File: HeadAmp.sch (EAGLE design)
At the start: 31 parts, among them U1 MAX97220A

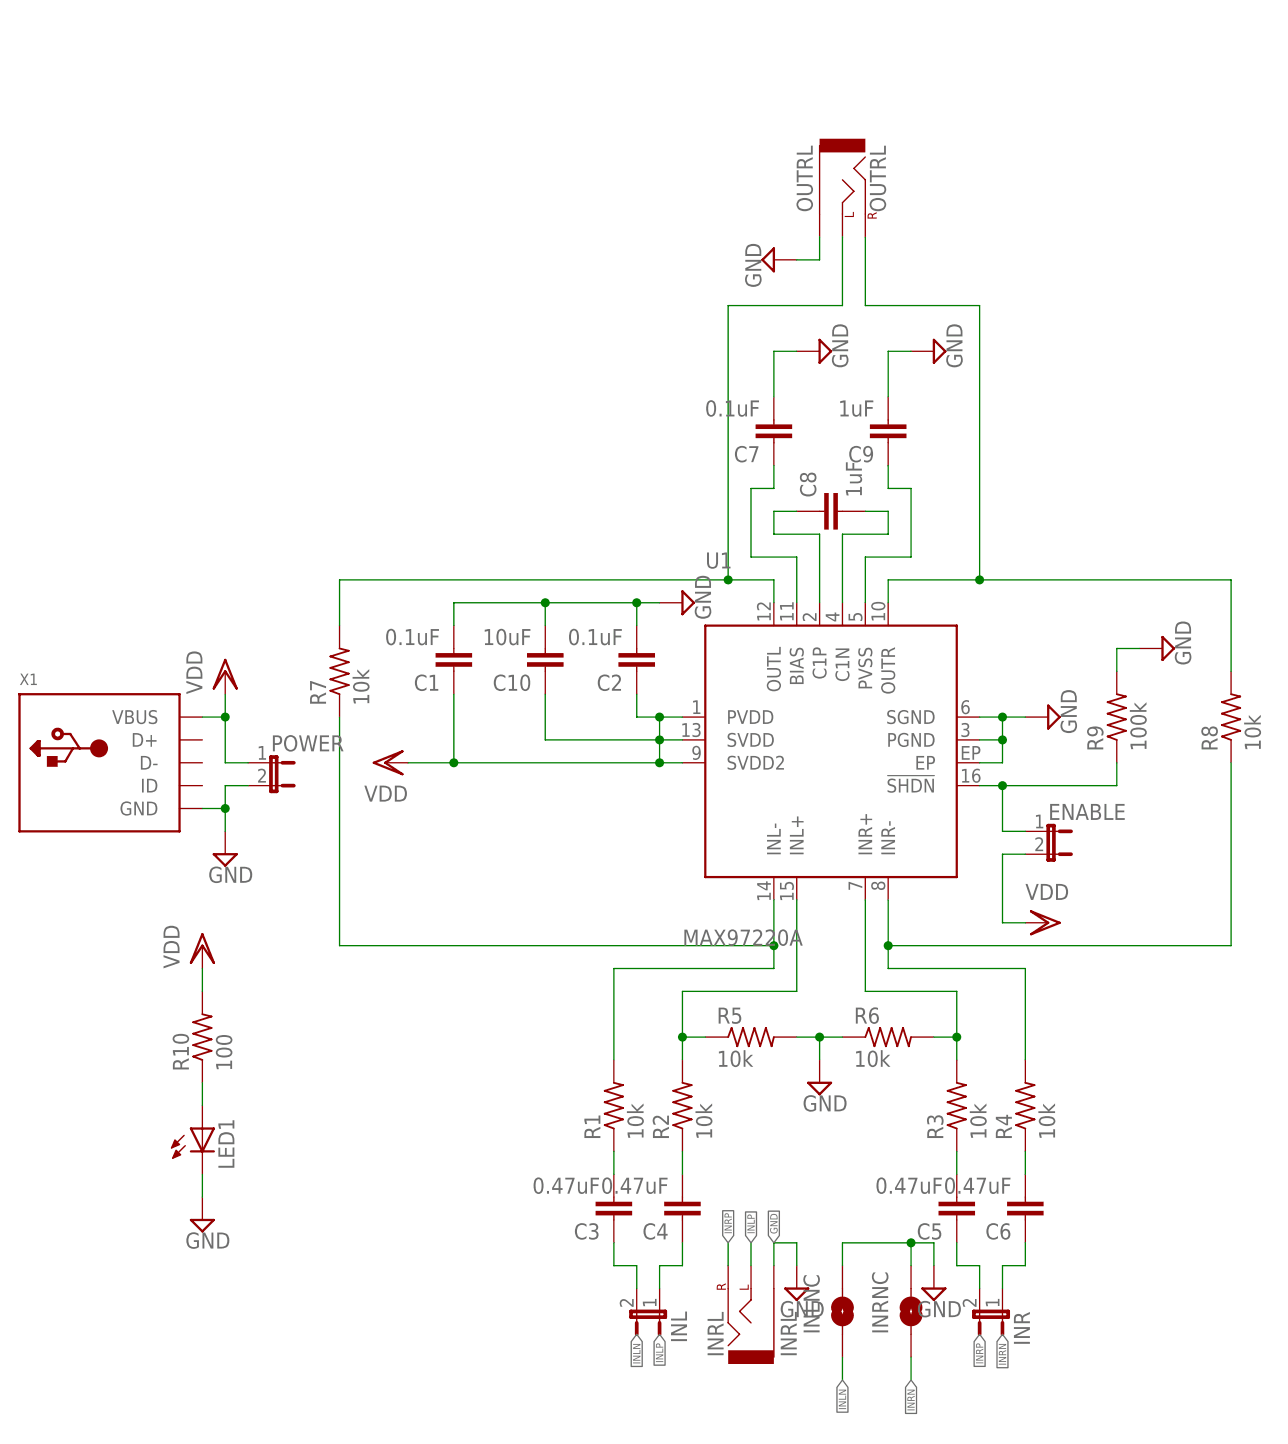
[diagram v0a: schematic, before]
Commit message: Changed Gain to Max
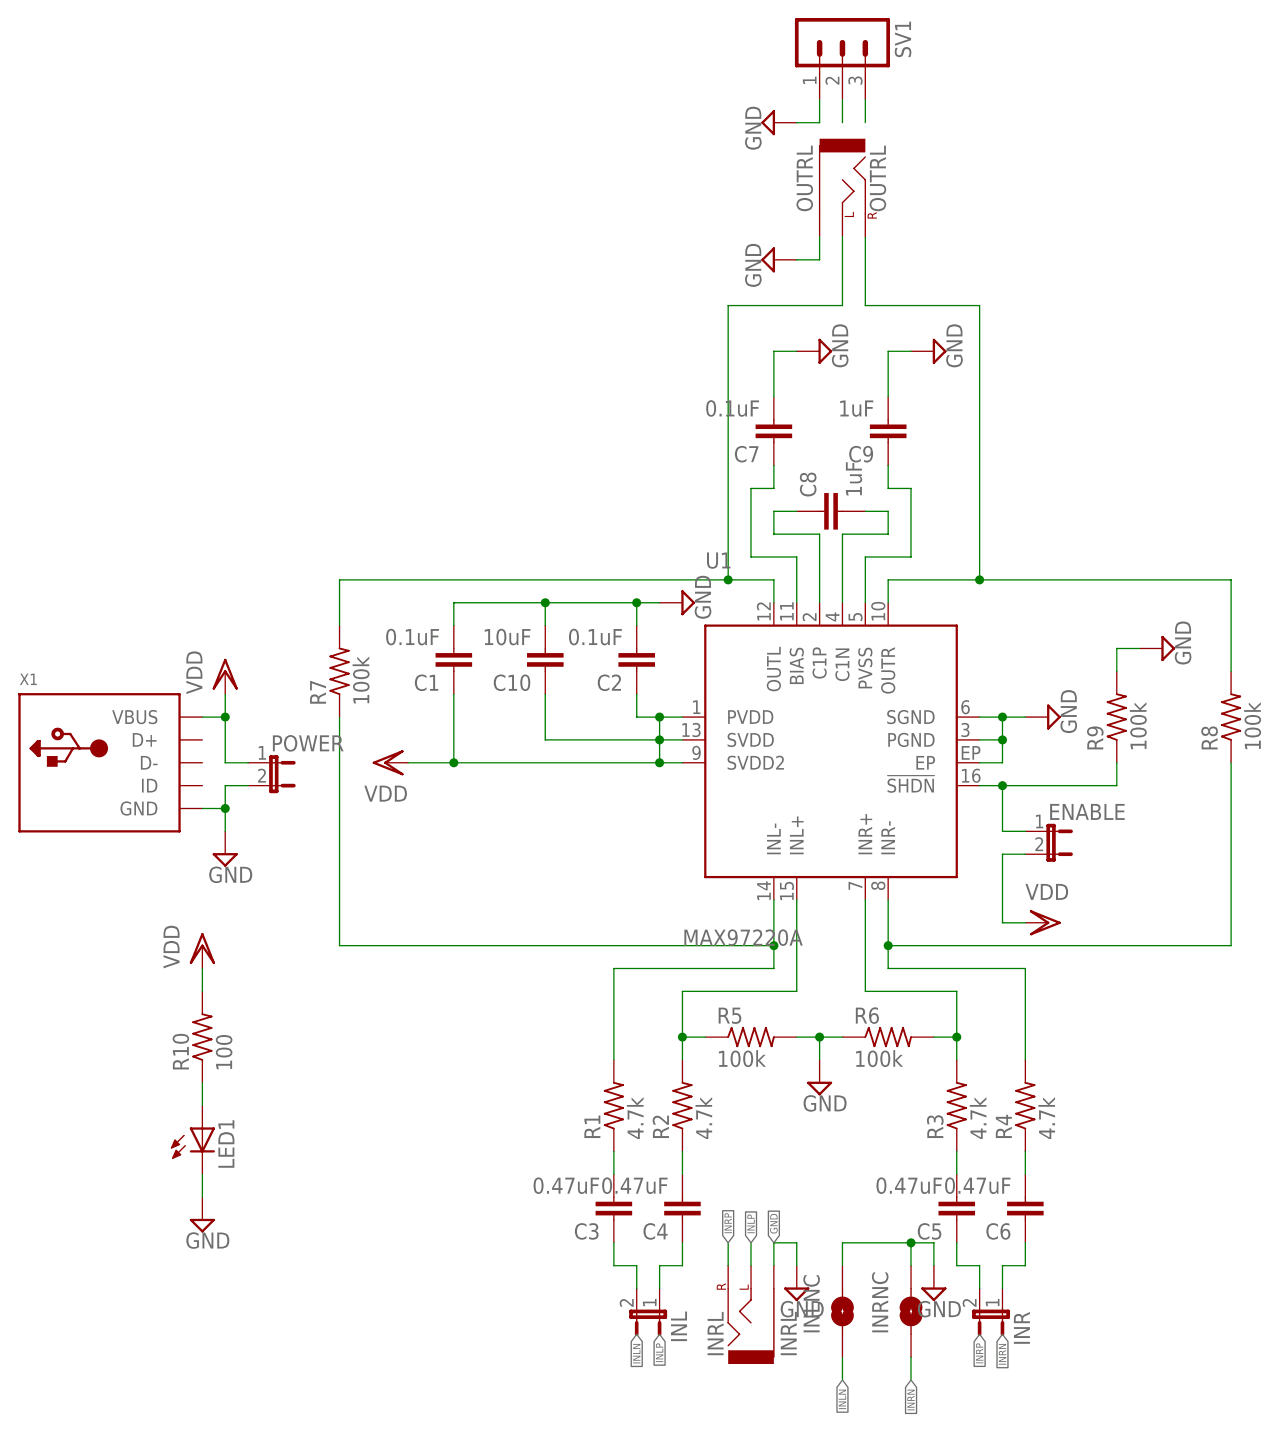
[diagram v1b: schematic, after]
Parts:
- added SV1: (no value), con-lstb:MA03-1
- R1, R2, R3, R4: value 10k -> 4.7k
- R5, R6, R7, R8: value 10k -> 100k
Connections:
- removed net N$5: OUTRL.1, R8.2, U1.OUTR
- removed net N$6: OUTRL.4, R7.2, U1.OUTL
- new net LOUT: OUTRL.4, R7.2, SV1.2, U1.OUTL
- new net ROUT: OUTRL.1, R8.2, SV1.3, U1.OUTR
- net GND: now also SV1.1
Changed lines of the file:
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@@
 <setting verticaltext="up"/>
 </settings>
-<grid distance="0.1" unitdist="inch" unit="inch" style="lines" multiple="1" display="yes" altdistance="0.01" altunitdist="inch" altunit="inch"/>
+<grid distance="0.1" unitdist="inch" unit="inch" style="lines" multiple="1" display="no" altdistance="0.01" altunitdist="inch" altunit="inch"/>
 <layers>
 <layer number="1" name="Top" color="4" fill="1" visible="no" active="no"/>
@@
 <parts>
 <part name="U1" library="maxim" deviceset="MAX97220A" device=""/>
-<part name="R1" library="rcl" deviceset="R-US_" device="R0603" value="10k"/>
-<part name="R2" library="rcl" deviceset="R-US_" device="R0603" value="10k"/>
-<part name="R3" library="rcl" deviceset="R-US_" device="R0603" value="10k"/>
-<part name="R4" library="rcl" deviceset="R-US_" device="R0603" value="10k"/>
-<part name="R5" library="rcl" deviceset="R-US_" device="R0603" value="10k"/>
-<part name="R6" library="rcl" deviceset="R-US_" device="R0603" value="10k"/>
-<part name="R7" library="rcl" deviceset="R-US_" device="R0603" value="10k"/>
-<part name="R8" library="rcl" deviceset="R-US_" device="R0603" value="10k"/>
+<part name="R1" library="rcl" deviceset="R-US_" device="R0603" value="4.7k"/>
+<part name="R2" library="rcl" deviceset="R-US_" device="R0603" value="4.7k"/>
+<part name="R3" library="rcl" deviceset="R-US_" device="R0603" value="4.7k"/>
+<part name="R4" library="rcl" deviceset="R-US_" device="R0603" value="4.7k"/>
+<part name="R5" library="rcl" deviceset="R-US_" device="R0603" value="100k"/>
+<part name="R6" library="rcl" deviceset="R-US_" device="R0603" value="100k"/>
+<part name="R7" library="rcl" deviceset="R-US_" device="R0603" value="100k"/>
+<part name="R8" library="rcl" deviceset="R-US_" device="R0603" value="100k"/>
 <part name="R9" library="rcl" deviceset="R-US_" device="R0603" value="100k"/>
 <part name="C1" library="rcl" deviceset="C-EU" device="C0603" value="0.1uF"/>
@@
 <part name="VDD1" library="supply1" deviceset="VDD" device=""/>
 <part name="SUPPLY11" library="supply2" deviceset="GND" device=""/>
+<part name="SV1" library="con-lstb" deviceset="MA03-1" device=""/>
+<part name="SUPPLY12" library="supply2" deviceset="GND" device=""/>
 </parts>
 <sheets>
@@
 <instance part="VDD1" gate="G$1" x="-45.72" y="0"/>
 <instance part="SUPPLY11" gate="GND" x="-45.72" y="-30.48"/>
+<instance part="SV1" gate="G$1" x="25.4" y="101.6" rot="R270"/>
+<instance part="SUPPLY12" gate="GND" x="17.78" y="91.44" rot="R270"/>
 </instances>
 <busses>
@@
 <wire x1="-45.72" y1="-25.4" x2="-45.72" y2="-27.94" width="0.1524" layer="91"/>
 </segment>
-</net>
-<net name="N$5" class="0">
+<segment>
+<pinref part="SUPPLY12" gate="GND" pin="GND"/>
+<pinref part="SV1" gate="G$1" pin="1"/>
+<wire x1="20.32" y1="91.44" x2="22.86" y2="91.44" width="0.1524" layer="91"/>
+<wire x1="22.86" y1="91.44" x2="22.86" y2="93.98" width="0.1524" layer="91"/>
+</segment>
+</net>
+<net name="ROUT" class="0">
 <segment>
 <pinref part="U1" gate="G$1" pin="OUTR"/>
@@
 <junction x="40.64" y="40.64"/>
 </segment>
-</net>
-<net name="N$6" class="0">
+<segment>
+<pinref part="SV1" gate="G$1" pin="3"/>
+<wire x1="27.94" y1="93.98" x2="27.94" y2="91.44" width="0.1524" layer="91"/>
+</segment>
+</net>
+<net name="LOUT" class="0">
 <segment>
 <pinref part="U1" gate="G$1" pin="OUTL"/>
@@
 <junction x="12.7" y="40.64"/>
 </segment>
-</net>
+<segment>
+<pinref part="SV1" gate="G$1" pin="2"/>
+<wire x1="25.4" y1="93.98" x2="25.4" y2="91.44" width="0.1524" layer="91"/>
+</segment>
+</net>
